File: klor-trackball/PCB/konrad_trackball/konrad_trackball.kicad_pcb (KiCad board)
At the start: 2 copper layers, 160 x 118.2 mm, 89 parts, among them J1 MJ-4PP-9, J2 Haptic Buzz, J3 lv27, SW1 SW_PUSH-MX_W_LED, SW10 SW_PUSH-MX_W_LED, SW11 SW_PUSH-MX_W_LED, SW12 SW_PUSH-MX_W_LED, SW13 SW_PUSH-MX_W_LED, SW14 SW_PUSH-MX_W_LED, SW15 SW_PUSH-MX_W_LED, SW16 SW_PUSH-MX_W_LED, SW17 SW_PUSH-MX_W_LED, SW18 RotaryEncoder_Switch, SW19 SW_PUSH-MX_W_LED, SW2 SW_PUSH-MX_W_LED, SW20 SW_PUSH-MX_W_LED, SW21 SW_PUSH-MX_W_LED, SW22 SW_PUSH-MX_W_LED, SW3 SW_PUSH-MX_W_LED, SW4 SW_PUSH-MX_W_LED, SW5 SW_PUSH-MX_W_LED, SW6 SW_PUSH-MX_W_LED, SW7 SW_PUSH-MX_W_LED, SW8 SW_PUSH-MX_W_LED, SW9 SW_PUSH-MX_W_LED, U1 ProMicro

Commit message: Task 3C: synchronize destructive PCB edits
* ci: stage Task 3C PCB generator

* task3c: add deterministic PCB synchronization transform

* task3c: generate synchronized PCB

* ci: retire Task 3B gate after PCB synchronization

* ci: retire one-shot Task 3C PCB generator

* task3c: add PCB synchronization preservation audit

* ci: audit Task 3C PCB synchronization

* fix: accept KiCad whitespace in Task 3C audit

* fix: allow trailing newline in Task 3C PCB audit

* ci: capture Task 3C audit diagnostics

* fix: parse mixed-indentation J4 footprint

* fix: correct Task 3C footprint regex escapes

* docs: record Task 3C PCB synchronization result

* docs: mark Task 3C complete and 3D next

* task3c: freeze PCB synchronization manifest

* docs: advance root status through Task 3C

* docs: describe Task 3C physical PCB state

* docs: advance engineering handoff through Task 3C

* docs: record Task 3C PCB state

* chore(klor): merge normalized stock PCB baseline

* chore(klor): normalize Task 3C PCB zone cache

* refactor(klor): rebaseline Task 3C transform

* test(klor): audit normalized Task 3C PCB

* docs(klor): record normalized Task 3C PCB

* docs(klor): merge Task 3C normalization policy

* docs(klor): merge Task 3C README with PCB normalization

* docs(klor): document normalized Task 3C derivative

* docs(klor): merge Task 3C plan with PCB normalization

* docs(klor): update normalized Task 3C geometry state

* docs(klor): update Task 3C handoff PCB blob

---------

Co-authored-by: github-actions[bot] <41898282+github-actions[bot]@users.noreply.github.com>
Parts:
- removed D22: D_Small, KLOR:Diode_SOD123
- removed SW22: SW_PUSH-MX_W_LED, KLOR:SK6812MINI_and_cherry_1
- added J4: PMW3360 Kivipallur, Connector_PinHeader_2.54mm:PinHeader_1x07_P2.54mm_Vertical, F.Cu at (60.0, 70.0)
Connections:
- J1 pad 3: RX -> (no net)
- SW14 pad 3: Net-(SW14B-DIN) -> Net-(SW13B-DOUT)
- U1 pad 12: AUDIO -> PMW_CS
- U1 pad 5: SDA -> PMW_SCK
- U1 pad 6: SCL -> PMW_MOSI
- U1 pad 7: RX -> PMW_MISO
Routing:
- net RX: track 82.7 -> 0.00 mm, vias 2 -> 0
- net Net-(SW14B-DIN): track 44.2 -> 0.00 mm, vias 2 -> 0
- net col1: track 294.6 -> 259.6 mm, vias 7 -> 6
- net AUDIO: track 103.2 -> 73.0 mm
- net Net-(SW13B-DOUT): track 44.6 -> 70.0 mm, vias 3 -> 4
- net Net-(D22-A): track 22.1 -> 0.00 mm, vias 1 -> 0
- net SDA: track 279.5 -> 258.1 mm
- net row3: track 166.7 -> 145.4 mm
- net SCL: track 260.6 -> 239.7 mm
- net PMW_SCK: track 0.00 -> 17.0 mm
- net PMW_MISO: track 0.00 -> 17.0 mm
- net PMW_CS: track 0.00 -> 17.0 mm
- net PMW_MOSI: track 0.00 -> 17.0 mm

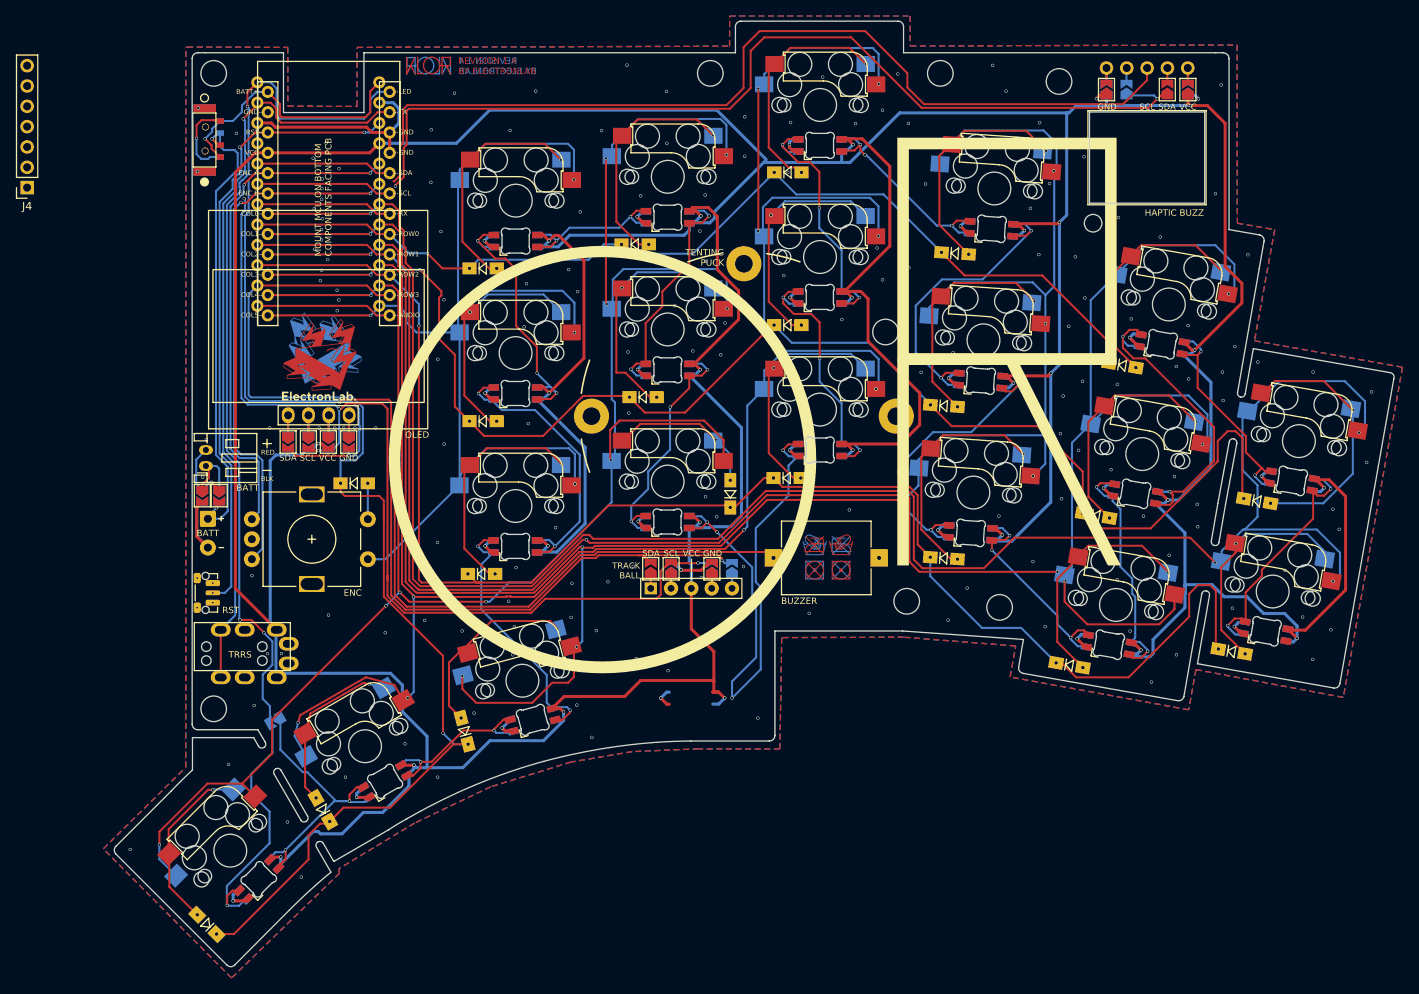
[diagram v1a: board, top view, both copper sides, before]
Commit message: task3d: place J4 and cut breakout pass-through
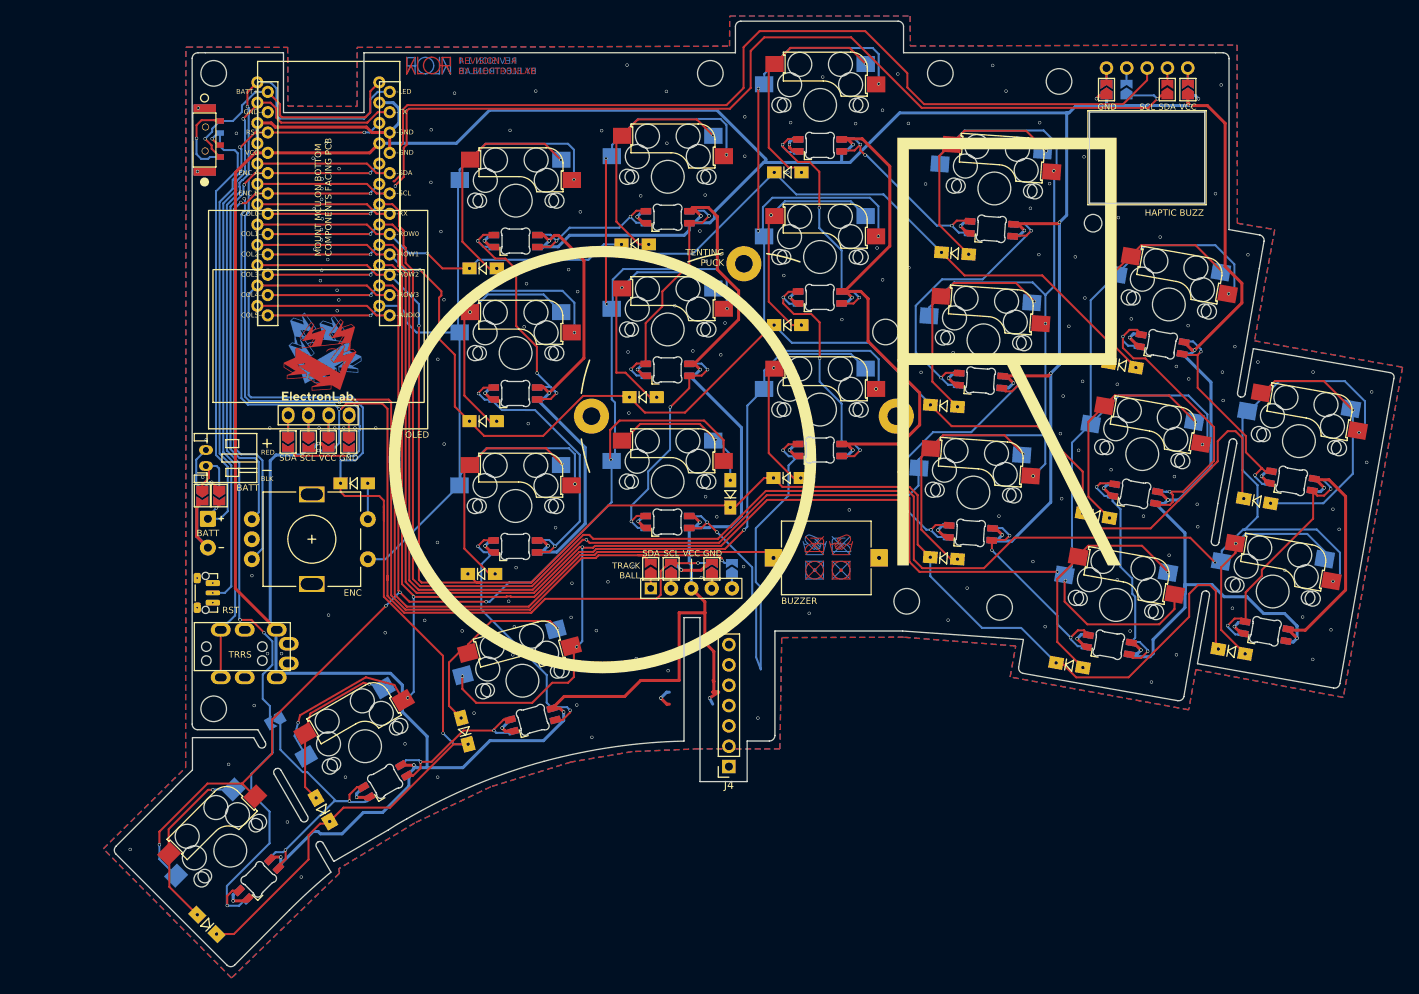
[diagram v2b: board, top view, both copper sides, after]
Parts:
- moved J4 113.7 mm to (147.7, 142.4)
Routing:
- net Net-(SW13B-DOUT): track 70.0 -> 60.1 mm, vias 4 -> 3
- net VCC: track 817.3 -> 824.1 mm
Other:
- outline, holes or cut-outs redrawn
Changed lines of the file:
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@@
 	(footprint "Connector_PinHeader_2.54mm:PinHeader_1x07_P2.54mm_Vertical"
         (layer "F.Cu")
-        (at 60 70)
+        (at 147.724665 142.367997)
         (descr "Through hole straight pin header, 1x07, 2.54mm pitch, single row")
         (tags "Through hole pin header THT 1x07 2.54mm single row")
@@
 	)
 	(gr_line
-		(start 142.967909 139.175891)
+		(start 142.111043 139.186691)
+		(end 142.111043 123.747997)
+		(stroke
+			(width 0.01)
+			(type solid)
+		)
+		(layer "Edge.Cuts")
+	)
+	(gr_line
+		(start 142.111043 123.747997)
+		(end 144.111043 123.747997)
+		(stroke
+			(width 0.01)
+			(type solid)
+		)
+		(layer "Edge.Cuts")
+	)
+	(gr_line
+		(start 144.111043 123.747997)
+		(end 144.111043 144.250000)
+		(stroke
+			(width 0.01)
+			(type solid)
+		)
+		(layer "Edge.Cuts")
+	)
+	(gr_line
+		(start 144.111043 144.250000)
+		(end 150.000000 144.250000)
+		(stroke
+			(width 0.01)
+			(type solid)
+		)
+		(layer "Edge.Cuts")
+	)
+	(gr_line
+		(start 150.000000 144.250000)
+		(end 150.000000 139.175891)
+		(stroke
+			(width 0.01)
+			(type solid)
+		)
+		(layer "Edge.Cuts")
+	)
+	(gr_line
+		(start 150.000000 139.175891)
 		(end 152.769828 139.175891)
 		(stroke
@@
 	(gr_curve
 		(pts
-			(xy 124.598127 141.714517) (xy 130.768401 140.057358) (xy 137.079705 139.211152) (xy 142.967909 139.175891)
+			(xy 124.598127 141.714517) (xy 130.470110 140.137470) (xy 136.469818 139.294864) (xy 142.111043 139.186691)
 		)
 		(stroke
@@
 	)
 	(segment
-        (start 148.115 131.73)
-        (end 148.109492 133.815508)
-        (width 0.254)
-        (layer "B.Cu")
-        (net 76)
-    )
+		(start 151.129969 128.715031)
+		(end 151.705 130.22)
+		(width 0.254)
+		(layer "B.Cu")
+		(net 76)
+	)
 	(via
 		(at 117.155 76.65)
@@
 	)
 	(segment
-		(start 143.03 125.171786)
-		(end 144.8905 127.032286)
-		(width 0.381)
-		(layer "F.Cu")
-		(net 3)
-	)
-	(segment
 		(start 102.824255 65.655745)
 		(end 104.02 64.46)
@@
 	)
 	(segment
-		(start 147.199492 133.815508)
-		(end 146.443984 133.06)
+		(start 146.443984 133.06)
+		(end 145.3 133.81)
 		(width 0.381)
 		(layer "F.Cu")
 		(net 3)
 	)
+	(via
+		(at 145.3 133.81)
+		(size 0.4)
+		(drill 0.3)
+		(layers "F.Cu" "B.Cu")
+		(net 3)
+	)
+	(segment
+		(start 145.3 133.81)
+		(end 145.701524 134.560002)
+		(width 0.381)
+		(layer "B.Cu")
+		(net 3)
+	)
 	(segment
 		(start 125.125 114.77)
@@
 	)
 	(segment
-		(start 143.03 120.1)
-		(end 143.03 125.171786)
-		(width 0.381)
-		(layer "F.Cu")
-		(net 3)
-	)
-	(segment
 		(start 161.729597 102.075688)
 		(end 162.404597 102.075688)
@@
 	)
 	(segment
-		(start 145.730675 131.61)
-		(end 136.695 131.61)
+		(start 136.695 131.61)
+		(end 141.5 131.61)
+		(width 0.381)
+		(layer "F.Cu")
+		(net 3)
+	)
+	(segment
+		(start 141.5 131.61)
+		(end 141.5 123.15)
+		(width 0.381)
+		(layer "F.Cu")
+		(net 3)
+	)
+	(segment
+		(start 141.5 123.15)
+		(end 144.72 123.15)
+		(width 0.381)
+		(layer "F.Cu")
+		(net 3)
+	)
+	(segment
+		(start 143.03 120.1)
+		(end 144.72 121.79)
+		(width 0.381)
+		(layer "F.Cu")
+		(net 3)
+	)
+	(segment
+		(start 144.72 121.79)
+		(end 144.72 123.15)
+		(width 0.381)
+		(layer "F.Cu")
+		(net 3)
+	)
+	(segment
+		(start 144.72 123.15)
+		(end 144.72 126.861786)
+		(width 0.381)
+		(layer "F.Cu")
+		(net 3)
+	)
+	(segment
+		(start 144.72 126.861786)
+		(end 144.8905 127.032286)
 		(width 0.381)
 		(layer "F.Cu")
@@
 	)
 	(via
-		(at 147.199492 133.815508)
-		(size 0.4)
-		(drill 0.3)
-		(layers "F.Cu" "B.Cu")
-		(free yes)
-		(net 3)
-	)
-	(via
 		(at 189.045 74.34)
 		(size 0.4)
@@
 	)
 	(segment
-		(start 147.199492 133.815508)
-		(end 146.454998 134.560002)
-		(width 0.381)
-		(layer "B.Cu")
-		(net 3)
-	)
-	(segment
 		(start 189.045 74.34)
 		(end 189.045 92.12)
@@
 	)
 	(segment
-		(start 146.454998 134.560002)
-		(end 145.701524 134.560002)
-		(width 0.381)
-		(layer "B.Cu")
-		(net 3)
-	)
-	(segment
 		(start 214.575 123.24)
 		(end 212.480161 121.145161)
@@
 	)
 	(segment
-		(start 148.115 131.73)
-		(end 151.129969 128.715031)
-		(width 0.254)
-		(layer "B.Cu")
-		(net 76)
-	)
-	(segment
 		(start 144.253986 111.080002)
 		(end 145.009492 111.835508)
@@
 	)
 	(via
-		(at 148.109492 133.815508)
-		(size 0.4)
-		(drill 0.3)
-		(layers "F.Cu" "B.Cu")
-		(net 76)
-	)
-	(via
 		(at 154.475 102.84)
 		(size 0.4)
@@
 	)
 	(segment
-		(start 151.705 130.22)
-		(end 148.109492 133.815508)
-		(width 0.254)
-		(layer "B.Cu")
-		(net 76)
-	)
-	(segment
 		(start 156.364473 103.550699)
 		(end 155.175 104.740172)
@@
 			"5a799d97-f593-4a83-a46e-0fe6a8aab313" "5ef44846-7962-4e98-bacb-786c92544aec"
 			"60ae76e2-11f9-4694-af72-db307b9ac206" "64d466a2-dcc0-4b8c-8837-aa4cfdb8d2eb"
-			"6a8d966a-c3bb-40c7-938f-b720f86fa562" "6bd36d23-f852-40e6-b4ea-d75a3117b622"
+			"3d3d0001-0000-4000-8000-000000000001" "3d3d0001-0000-4000-8000-000000000002" "3d3d0001-0000-4000-8000-000000000003" "3d3d0001-0000-4000-8000-000000000004" "3d3d0001-0000-4000-8000-000000000005" "3d3d0001-0000-4000-8000-000000000006" "6bd36d23-f852-40e6-b4ea-d75a3117b622"
 			"6fd13230-0b3e-490a-bd58-2f90e4c84c7b" "6fdccc28-c985-4fd0-8e49-c7cb435b55af"
 			"7acd7714-37b4-47a0-92aa-c2be807d5b74" "7b74714f-72f2-45fe-b8d7-ad6140b15429"

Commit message: task3e: generate PMW routing
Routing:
- net PMW_CS: track 17.0 -> 184.2 mm, vias 0 -> 11
- net PMW_MOSI: track 17.0 -> 143.1 mm, vias 0 -> 4
- net PMW_SCK: track 17.0 -> 137.3 mm, vias 0 -> 10
- net PMW_MISO: track 17.0 -> 115.5 mm, vias 0 -> 2
- net GND: track 113.4 -> 124.1 mm
- net VCC: track 824.1 -> 826.6 mm
